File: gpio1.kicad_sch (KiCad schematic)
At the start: 2 parts, among them U27 RK3576

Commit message: Add files via upload
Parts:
- renumbered C325 to C98, U27 to U2
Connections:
- net BT_CTRL renamed HOST_WAKE_BT_H
- net PCM_CLK renamed SAI2_SCLK_M0
- net PCM_IN renamed SAI2_SDI_M0
- net PCM_OUT renamed SAI2_SDO_M0
- net PCM_SYNC renamed SAI2_LRCK_M0
- net SDIO_CLK renamed SDMMC1_CLK_M0
- net SDIO_CMD renamed SDMMC1_CMD_M0
- net SDIO_D0 renamed SDMMC1_D1_M0
- net SDIO_D1 renamed SDMMC1_D0_M0
- net SDIO_D2 renamed SDMMC1_D2_M0
- net SDIO_D3 renamed SDMMC1_D3_M0
- net UART_CST renamed UART4_CTSN_M1
- net UART_RST renamed UART4_RTSN_M1
- net UART_RX renamed UART4_TX_M1
- net UART_TX renamed UART4_RX_M1
- net WIIFI_HOST_WAKE renamed BT_REG_ON_H
- net WIIFI_REG_ON renamed WIFI_REG_ON_H

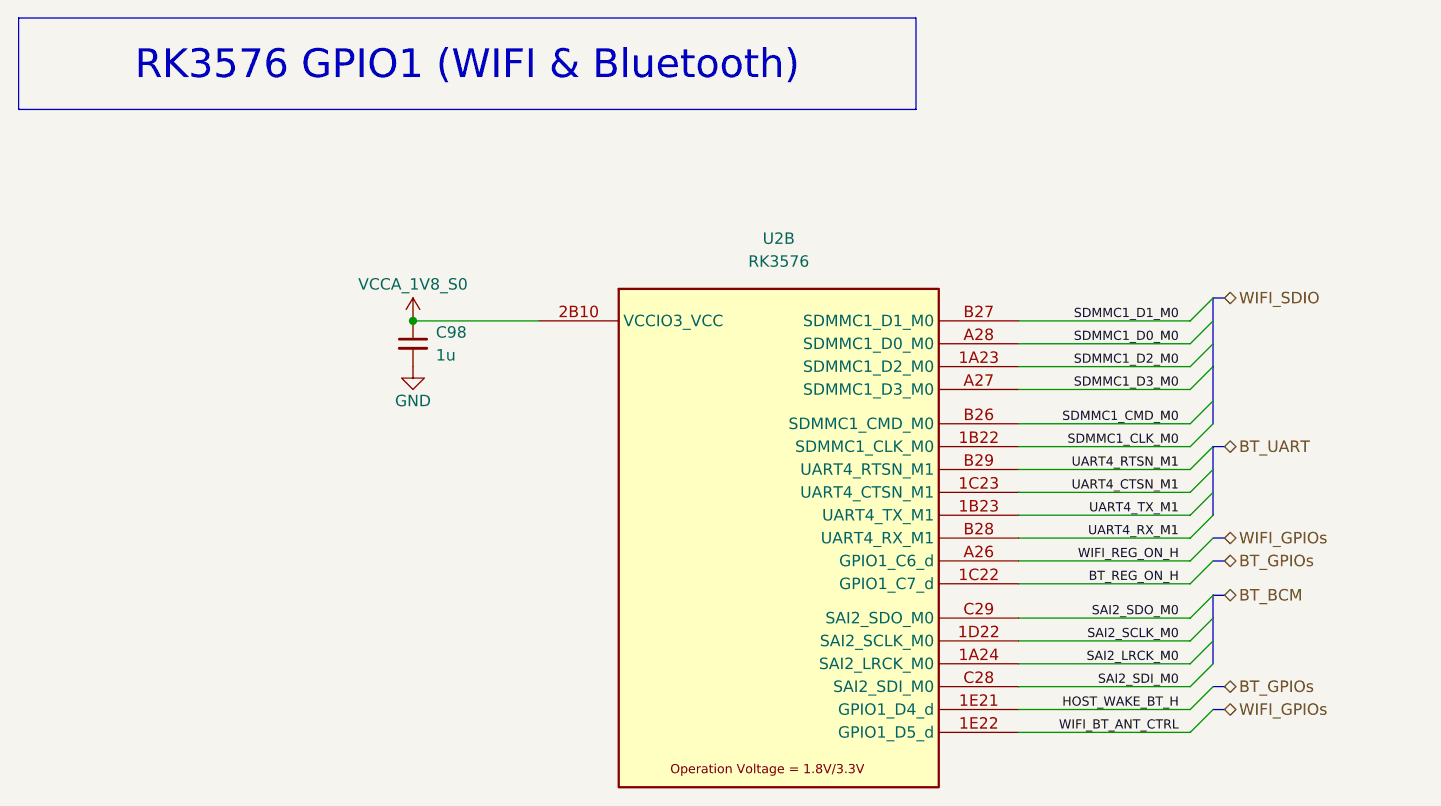
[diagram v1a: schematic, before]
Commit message: SBC Board V0.2
The SBC schematics before footprint and part number check
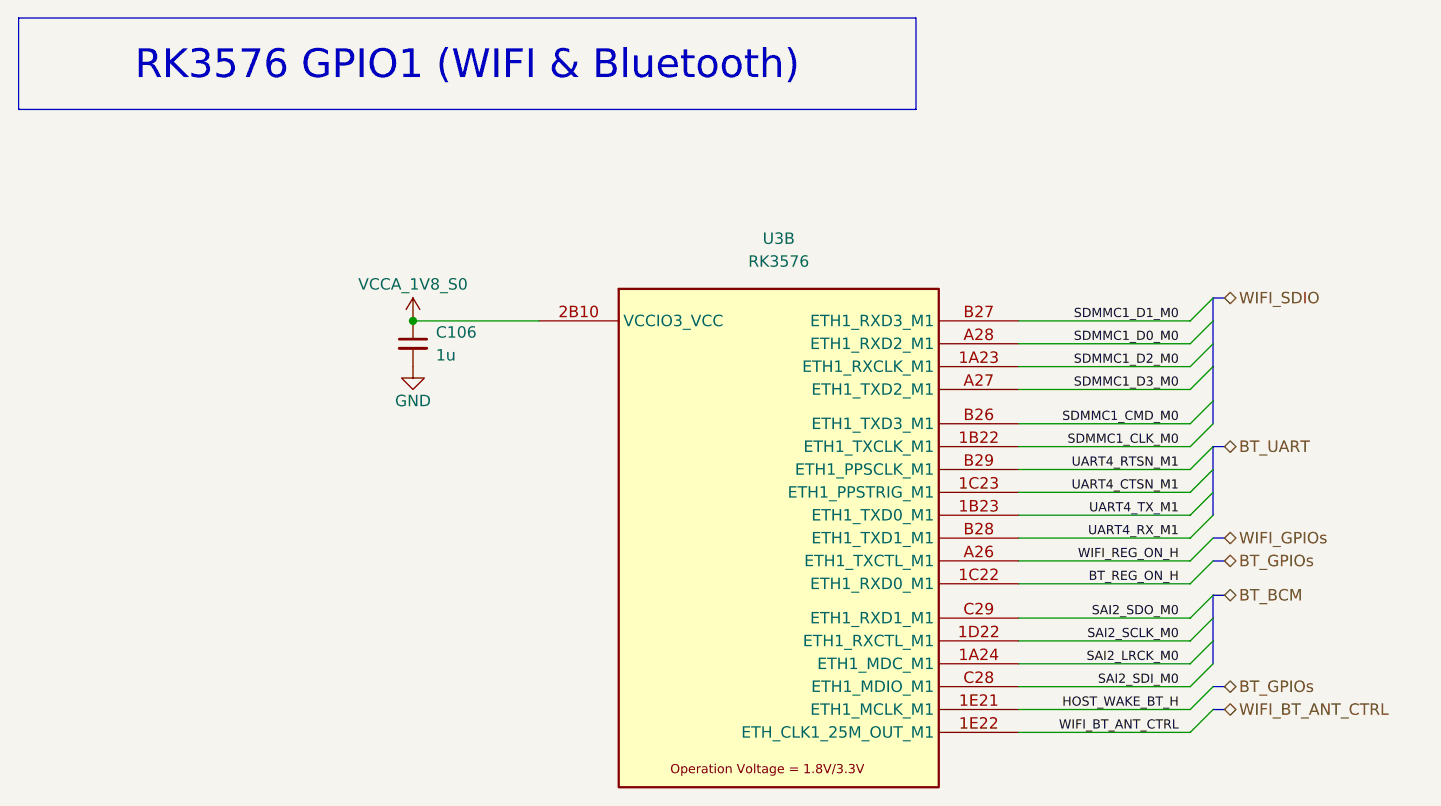
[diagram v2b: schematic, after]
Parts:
- U3: renamed from U2; footprint (none) -> easyeda2kicad:FCCSP-698_L17.2-W16.1-TL_RK3576
- renumbered C98 to C106
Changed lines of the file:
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@@
 		)
 	)
-	(hierarchical_label "WIFI_GPIOs"
+	(hierarchical_label "WIFI_BT_ANT_CTRL"
 		(shape bidirectional)
 		(at 146.05 88.9 0)
@@
 		(in_pos_files yes)
 		(dnp no)
-		(property "Reference" "#PWR0134"
+		(property "Reference" "#PWR0146"
 			(at 55.88 49.53 0)
 			(hide yes)
@@
 			(project "RK3576 SBC"
 				(path "/b79dbff4-0cad-4ff7-bec2-7c0e4f8b14d3/34f9b0cb-aeae-42b4-a2af-a0a79afcf392/758a90de-94a4-4b45-a7ba-61e4621900fd"
-					(reference "#PWR0134")
+					(reference "#PWR0146")
 					(unit 1)
 				)
@@
 		(in_pos_files yes)
 		(dnp no)
-		(property "Reference" "U2"
+		(property "Reference" "U3"
 			(at 96.52 36.576 0)
 			(show_name no)
@@
 			)
 		)
-		(property "Footprint" ""
+		(property "Footprint" "easyeda2kicad:FCCSP-698_L17.2-W16.1-TL_RK3576"
 			(at 29.21 6.985 0)
 			(hide yes)
@@
 		)
 		(pin "1A23"
-			(alternate "SDMMC1_D2_M0")
 		)
 		(pin "1A24"
-			(alternate "SAI2_LRCK_M0")
 		)
 		(pin "1B22"
-			(alternate "SDMMC1_CLK_M0")
 		)
 		(pin "1B23"
-			(alternate "UART4_TX_M1")
 		)
 		(pin "1A17"
 		)
 		(pin "B28"
-			(alternate "UART4_RX_M1")
 		)
 		(pin "C28"
-			(alternate "SAI2_SDI_M0")
 		)
 		(pin "1C22"
-			(alternate "GPIO1_C7_d")
 		)
 		(pin "1E21"
-			(alternate "GPIO1_D4_d")
 		)
 		(pin "B27"
-			(alternate "SDMMC1_D1_M0")
 		)
 		(pin "B26"
-			(alternate "SDMMC1_CMD_M0")
 		)
 		(pin "1A13"
@@
 		)
 		(pin "B29"
-			(alternate "UART4_RTSN_M1")
 		)
 		(pin "1D18"
@@
 		)
 		(pin "A26"
-			(alternate "GPIO1_C6_d")
 		)
 		(pin "1C23"
-			(alternate "UART4_CTSN_M1")
 		)
 		(pin "A27"
-			(alternate "SDMMC1_D3_M0")
 		)
 		(pin "A28"
-			(alternate "SDMMC1_D0_M0")
 		)
 		(pin "C29"
-			(alternate "SAI2_SDO_M0")
 		)
 		(pin "1D22"
-			(alternate "SAI2_SCLK_M0")
 		)
 		(pin "1A14"
 		)
 		(pin "1E22"
-			(alternate "GPIO1_D5_d")
 		)
 		(pin "1A18"
@@
 			(project "RK3576 SBC"
 				(path "/b79dbff4-0cad-4ff7-bec2-7c0e4f8b14d3/34f9b0cb-aeae-42b4-a2af-a0a79afcf392/758a90de-94a4-4b45-a7ba-61e4621900fd"
-					(reference "U2")
+					(reference "U3")
 					(unit 2)
 				)
@@
 		(in_pos_files yes)
 		(dnp no)
-		(property "Reference" "#PWR0135"
+		(property "Reference" "#PWR0147"
 			(at 55.88 57.15 0)
 			(hide yes)
@@
 			(project "RK3576 SBC"
 				(path "/b79dbff4-0cad-4ff7-bec2-7c0e4f8b14d3/34f9b0cb-aeae-42b4-a2af-a0a79afcf392/758a90de-94a4-4b45-a7ba-61e4621900fd"
-					(reference "#PWR0135")
+					(reference "#PWR0147")
 					(unit 1)
 				)
@@
 		(dnp no)
 		(fields_autoplaced yes)
-		(property "Reference" "C98"
+		(property "Reference" "C106"
 			(at 58.42 46.9962 0)
 			(show_name no)
@@
 			(project "RK3576 SBC"
 				(path "/b79dbff4-0cad-4ff7-bec2-7c0e4f8b14d3/34f9b0cb-aeae-42b4-a2af-a0a79afcf392/758a90de-94a4-4b45-a7ba-61e4621900fd"
-					(reference "C98")
+					(reference "C106")
 					(unit 1)
 				)

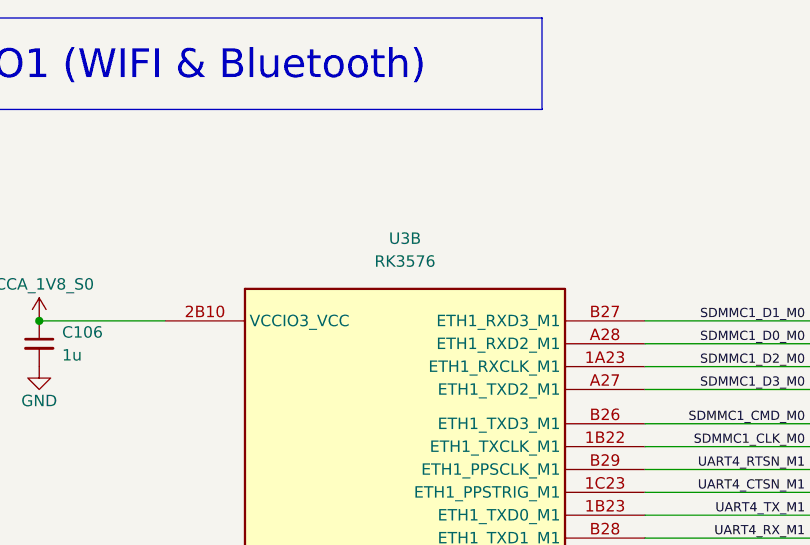
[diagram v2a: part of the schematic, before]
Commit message: SBCv0.3
there is no big thing update just some LCSC & Mouser parts
and Big problem deleted alot of component values (:
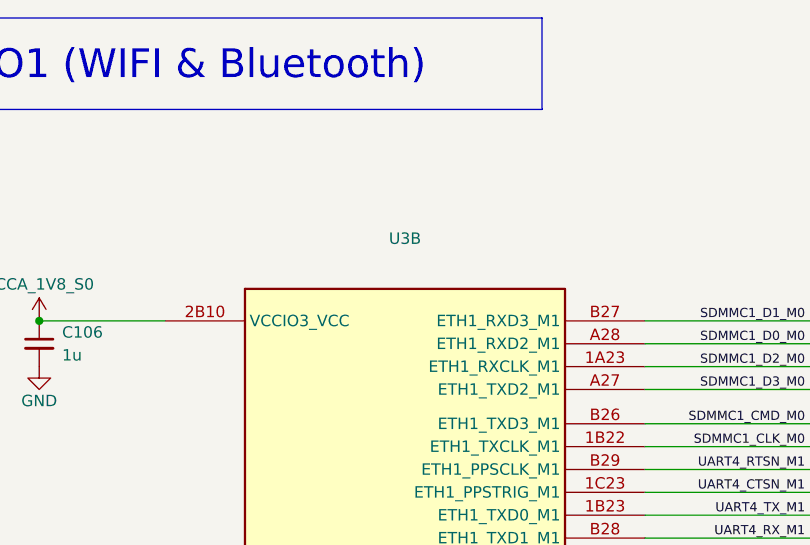
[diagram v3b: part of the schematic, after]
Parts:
- C106: footprint Capacitor_SMD:C_0402_1005Metric_Pad0.74x0.62mm_HandSolder -> Capacitor_SMD:C_0201_0603Metric_Pad0.64x0.40mm_HandSolder; LCSC Part (none) -> C5209398; Mouser Part (none) -> CL03A105KP3NSNC
- U3: value RK3576 -> (none); LCSC Part (none) -> (polyline
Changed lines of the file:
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@@
 			)
 		)
-		(property "Value" "RK3576"
+		(property "Value" ""
 			(at 96.52 39.116 0)
 			(show_name no)
@@
 			)
 		)
-		(property "KLC_S5.1" ""
+		(property "LCSC Part" "(polyline"
+			(at 96.52 69.85 0)
+			(hide yes)
+			(show_name no)
+			(do_not_autoplace no)
+			(effects
+				(font
+					(size 1.27 1.27)
+				)
+			)
+		)
+		(property "KLC_S4.2_DVDD" ""
+			(at 96.52 69.85 0)
+			(hide yes)
+			(show_name no)
+			(do_not_autoplace no)
+			(effects
+				(font
+					(size 1.27 1.27)
+				)
+			)
+		)
+		(property "KLC_S4.2_VREG_LX" ""
 			(at 96.52 69.85 0)
 			(hide yes)
@@
 					(reference "U3")
 					(unit 2)
+					(variant
+						(name "Test")
+					)
 				)
 			)
@@
 			)
 		)
-		(property "Footprint" "Capacitor_SMD:C_0402_1005Metric_Pad0.74x0.62mm_HandSolder"
+		(property "Footprint" "Capacitor_SMD:C_0201_0603Metric_Pad0.64x0.40mm_HandSolder"
 			(at 55.88 48.26 0)
 			(hide yes)
@@
 			)
 		)
-		(property "KLC_S5.1" ""
+		(property "LCSC Part" "C5209398"
+			(at 55.88 48.26 0)
+			(hide yes)
+			(show_name no)
+			(do_not_autoplace no)
+			(effects
+				(font
+					(size 1.27 1.27)
+				)
+			)
+		)
+		(property "Mouser Part" "CL03A105KP3NSNC "
+			(at 55.88 48.26 0)
+			(hide yes)
+			(show_name no)
+			(do_not_autoplace no)
+			(effects
+				(font
+					(size 1.27 1.27)
+				)
+			)
+		)
+		(property "KLC_S4.2_DVDD" ""
+			(at 55.88 48.26 0)
+			(hide yes)
+			(show_name no)
+			(do_not_autoplace no)
+			(effects
+				(font
+					(size 1.27 1.27)
+				)
+			)
+		)
+		(property "KLC_S4.2_VREG_LX" ""
 			(at 55.88 48.26 0)
 			(hide yes)
@@
 					(reference "C106")
 					(unit 1)
-				)
-			)
+					(variant
+						(name "Test")
+					)
+				)
+			)

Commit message: SBCv0.4
add LCSC & Mouser parts 
and solve the deleted value in the past version
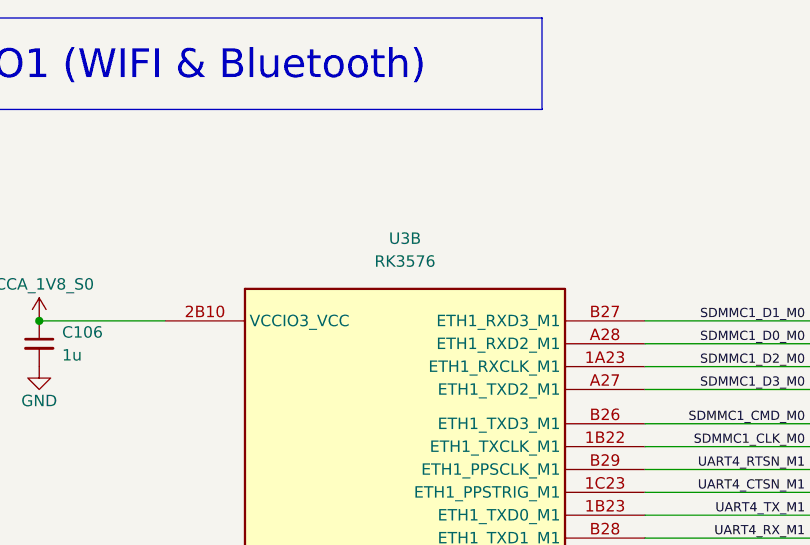
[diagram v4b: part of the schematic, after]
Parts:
- U3: value (none) -> RK3576; LCSC Part (polyline -> C42388007
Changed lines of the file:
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@@
 			)
 		)
-		(property "Value" ""
+		(property "Value" "RK3576"
 			(at 96.52 39.116 0)
 			(show_name no)
@@
 			)
 		)
-		(property "LCSC Part" "(polyline"
+		(property "LCSC Part" "C42388007"
 			(at 96.52 69.85 0)
 			(hide yes)
